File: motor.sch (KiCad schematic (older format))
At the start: 46 parts, among them J16 70543-0003, Q10 PMPB20EN, Q3 PMPB20EN, Q4 PMPB20EN, Q5 PMPB20EN, Q6 PMPB20EN, Q7 PMPB20EN, Q8 PMPB20EN, Q9 PMPB20EN, U6 TMC2160-TA

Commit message: Current snapshot
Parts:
- removed R24: 47k, Resistor_SMD:R_0603_1608Metric, symbol Device:R
- removed R35, R36: 0.15, Resistor_SMD:R_2512_6332Metric, symbol Device:R
- added C41: 100uF, Capacitor_SMD:CP_Elec_6.3x5.7, symbol Device:CP
- C35: renamed from C36; value 220uF -> 100uF; footprint Capacitor_SMD:CP_Elec_8x10 -> Capacitor_SMD:CP_Elec_6.3x5.7
- R32: renamed from R33; value 0.15 -> 0.75; Note (none) -> 0.5 or 1W
- R33: renamed from R34; value 0.15 -> 0.75; Note (none) -> 0.5W or 1W
- renumbered C35 to C34, C37 to C36, C38 to C37, C39 to C38, C40 to C39, C41 to C40, R25 to R24, R26 to R25, R27 to R26, R28 to R27, R29 to R28, R30 to R29, R31 to R30, R32 to R31, R37 to R34, R38 to R35, R39 to R36, R40 to R37
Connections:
- net EN is gone; now on net GND: U6.28 (DRV_ENN)
- net VDD_PWR is gone; now on net VDD24V: D21.1 (K)
- net GND: now also C37.2, C41.2
- net GNDA: no longer C37.2
- net VDD24V: now also C41.1
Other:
- note added: "0.075 Ohm = RMS 3.1A"
- note removed: "0.07 Ohm = RMS 3.4A"

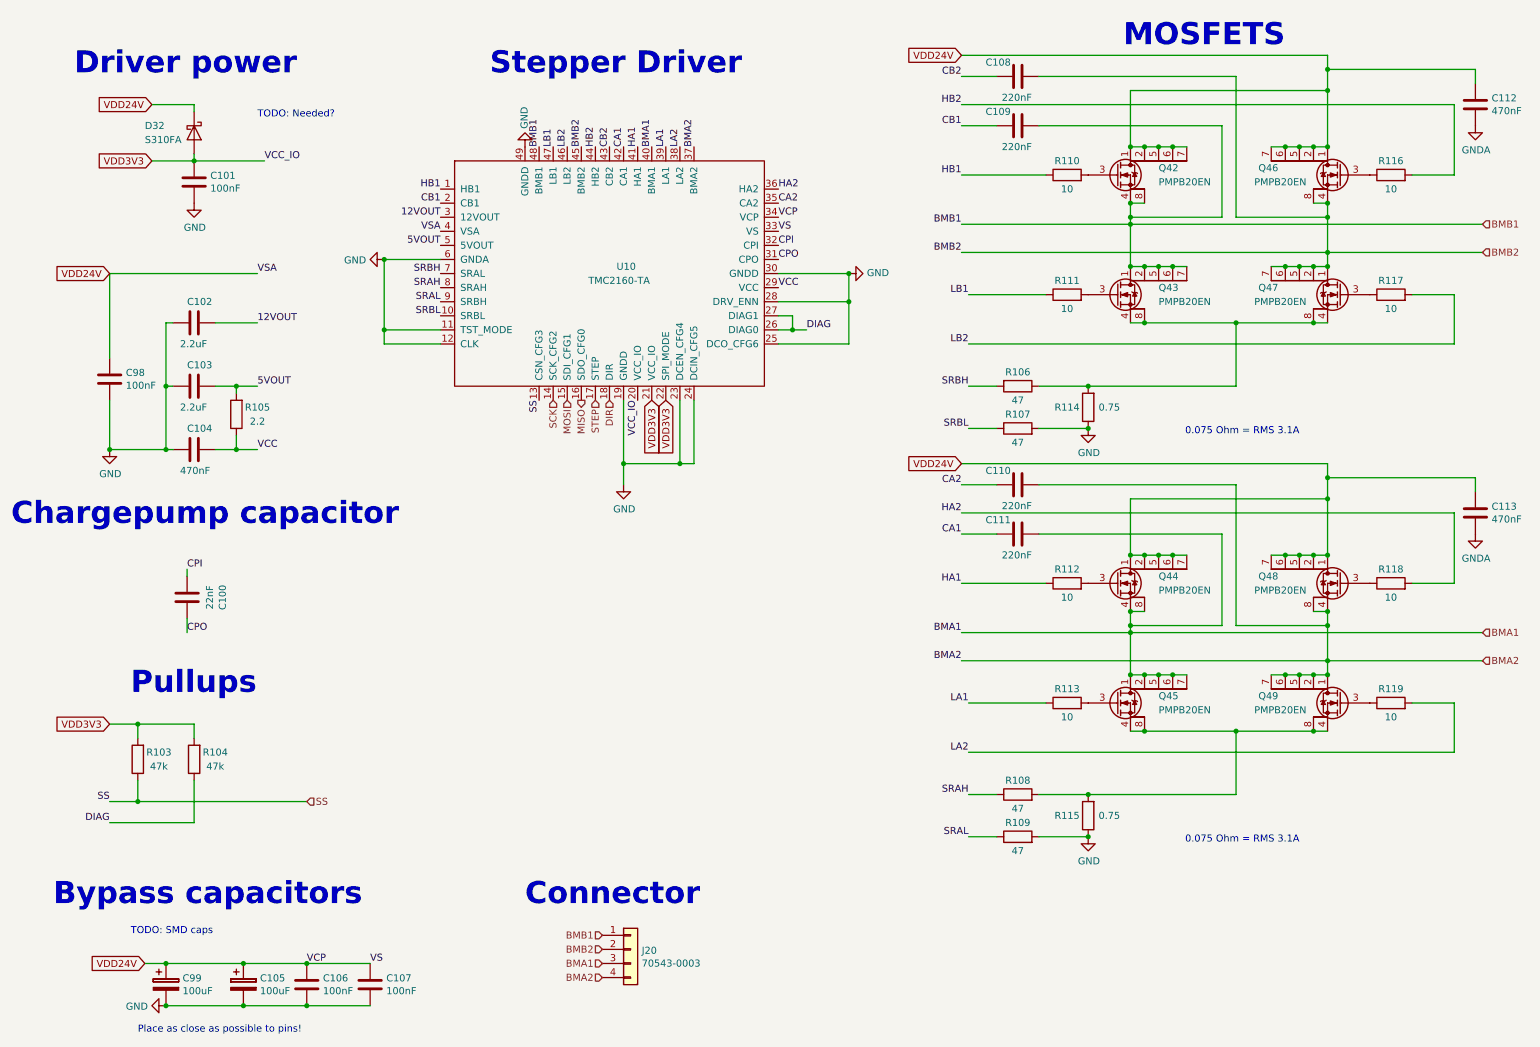
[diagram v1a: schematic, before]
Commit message: Finished general layout and power planes
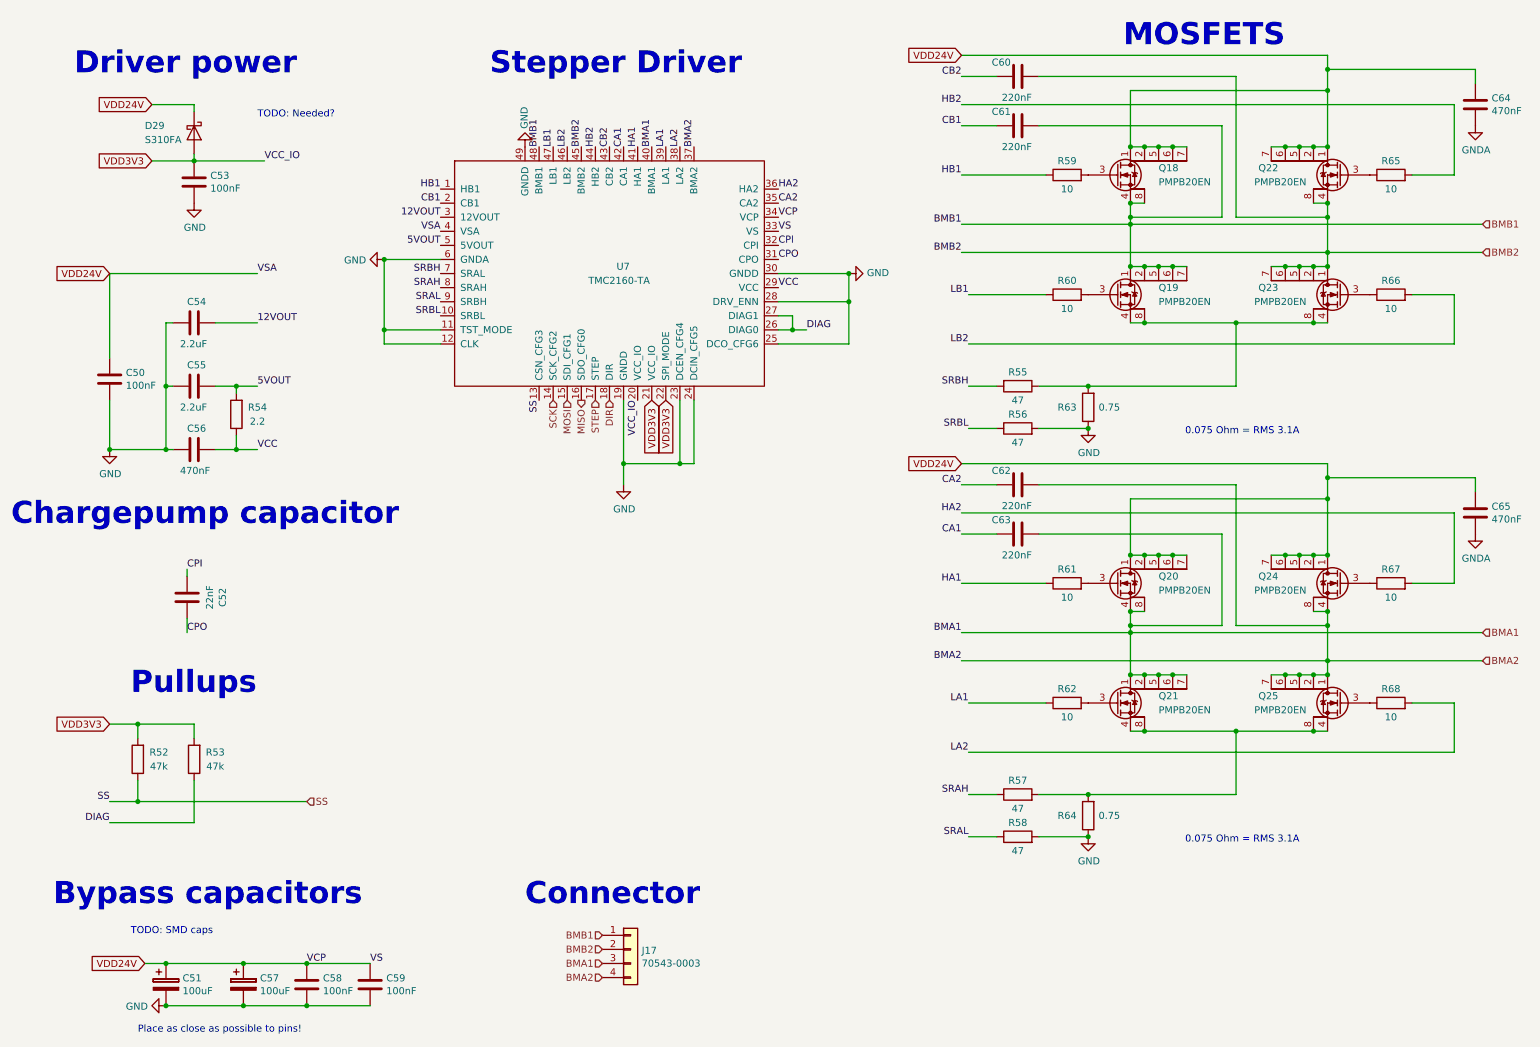
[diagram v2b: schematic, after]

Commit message: Add SD card reader, placed temp connections, fixed stepper placement
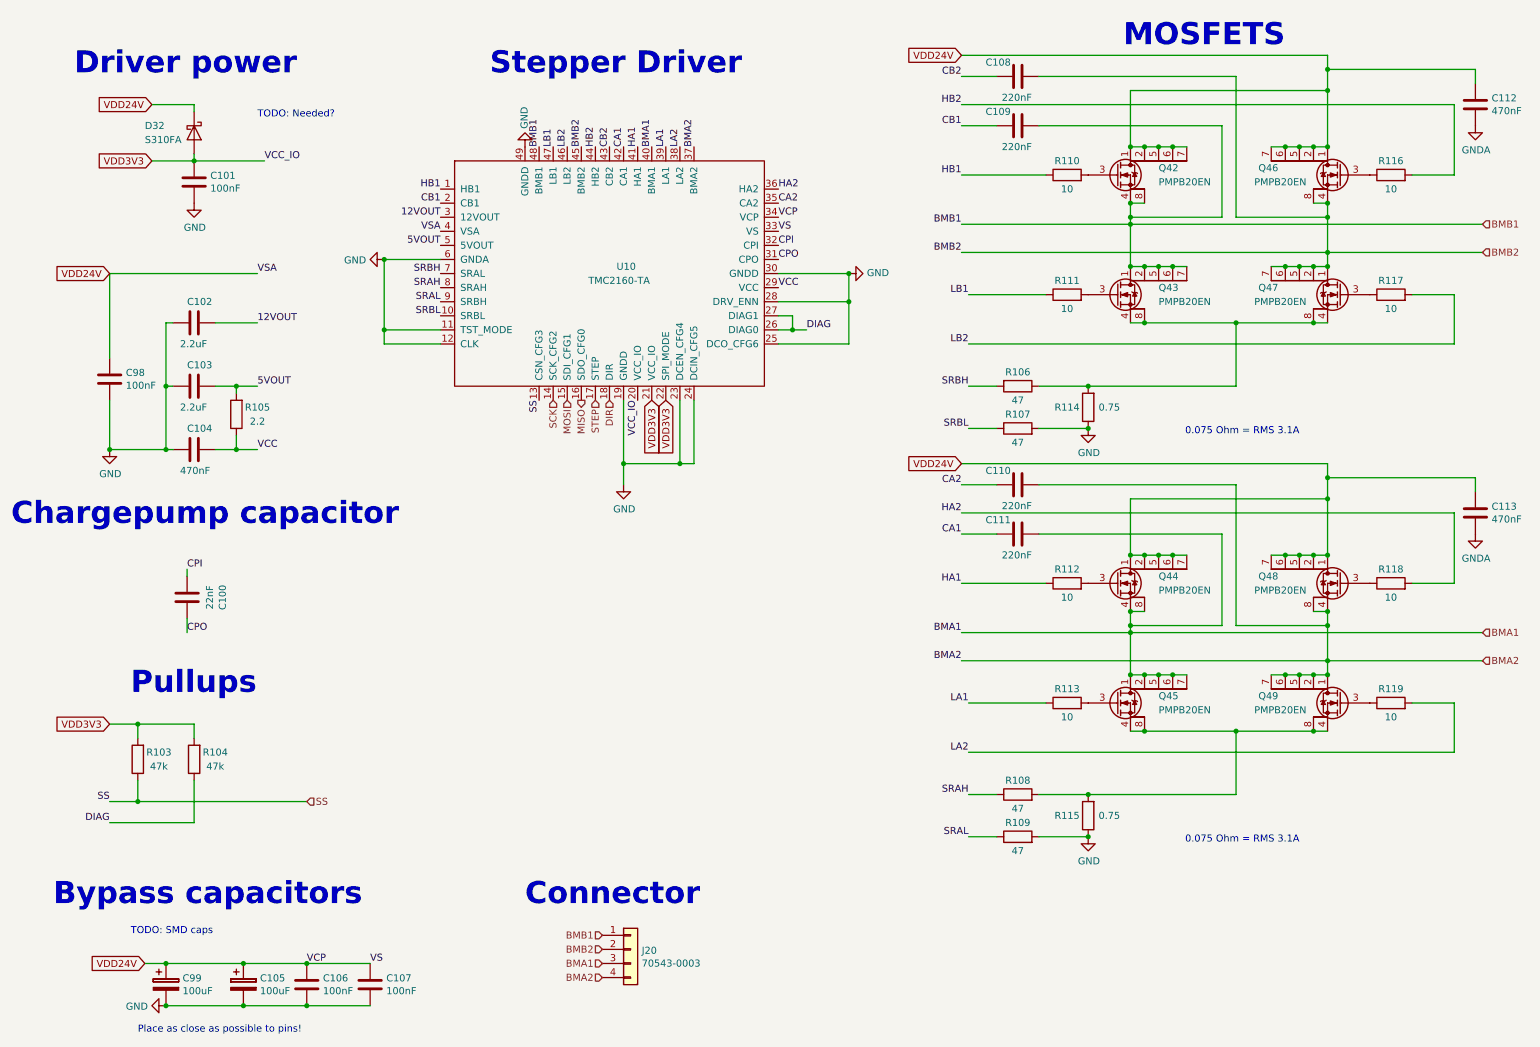
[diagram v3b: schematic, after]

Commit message: Placed some bypass caps
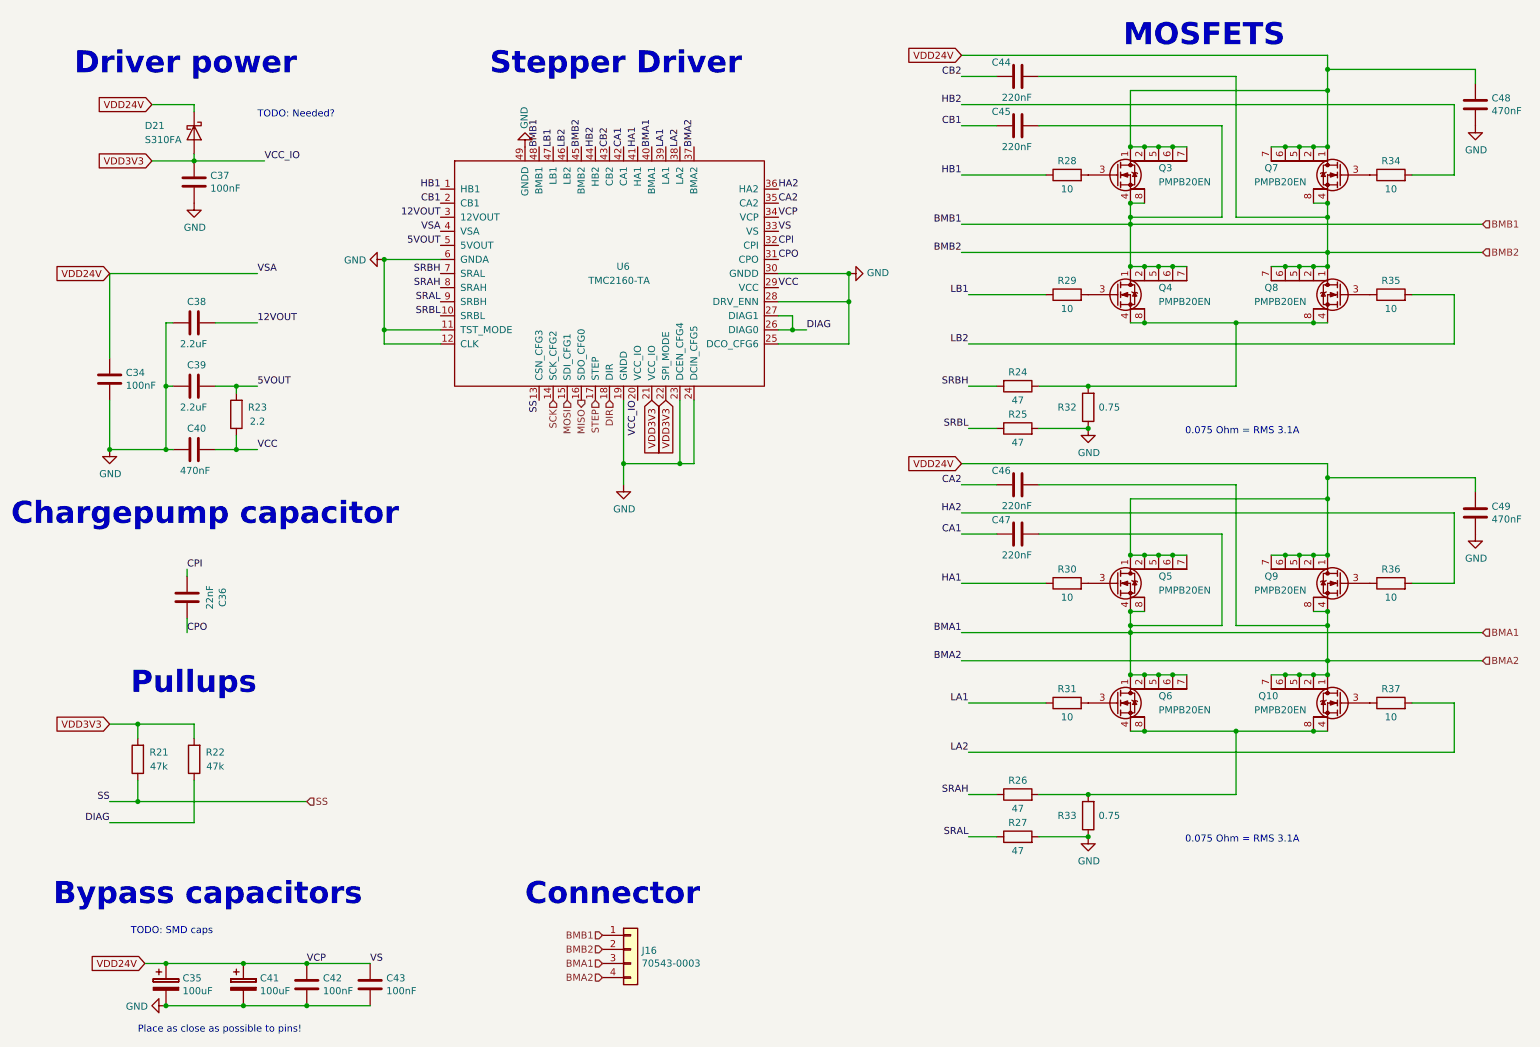
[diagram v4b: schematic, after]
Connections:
- net GNDA is gone; now on net GND: C48.2, C49.2

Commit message: Placed last connectors
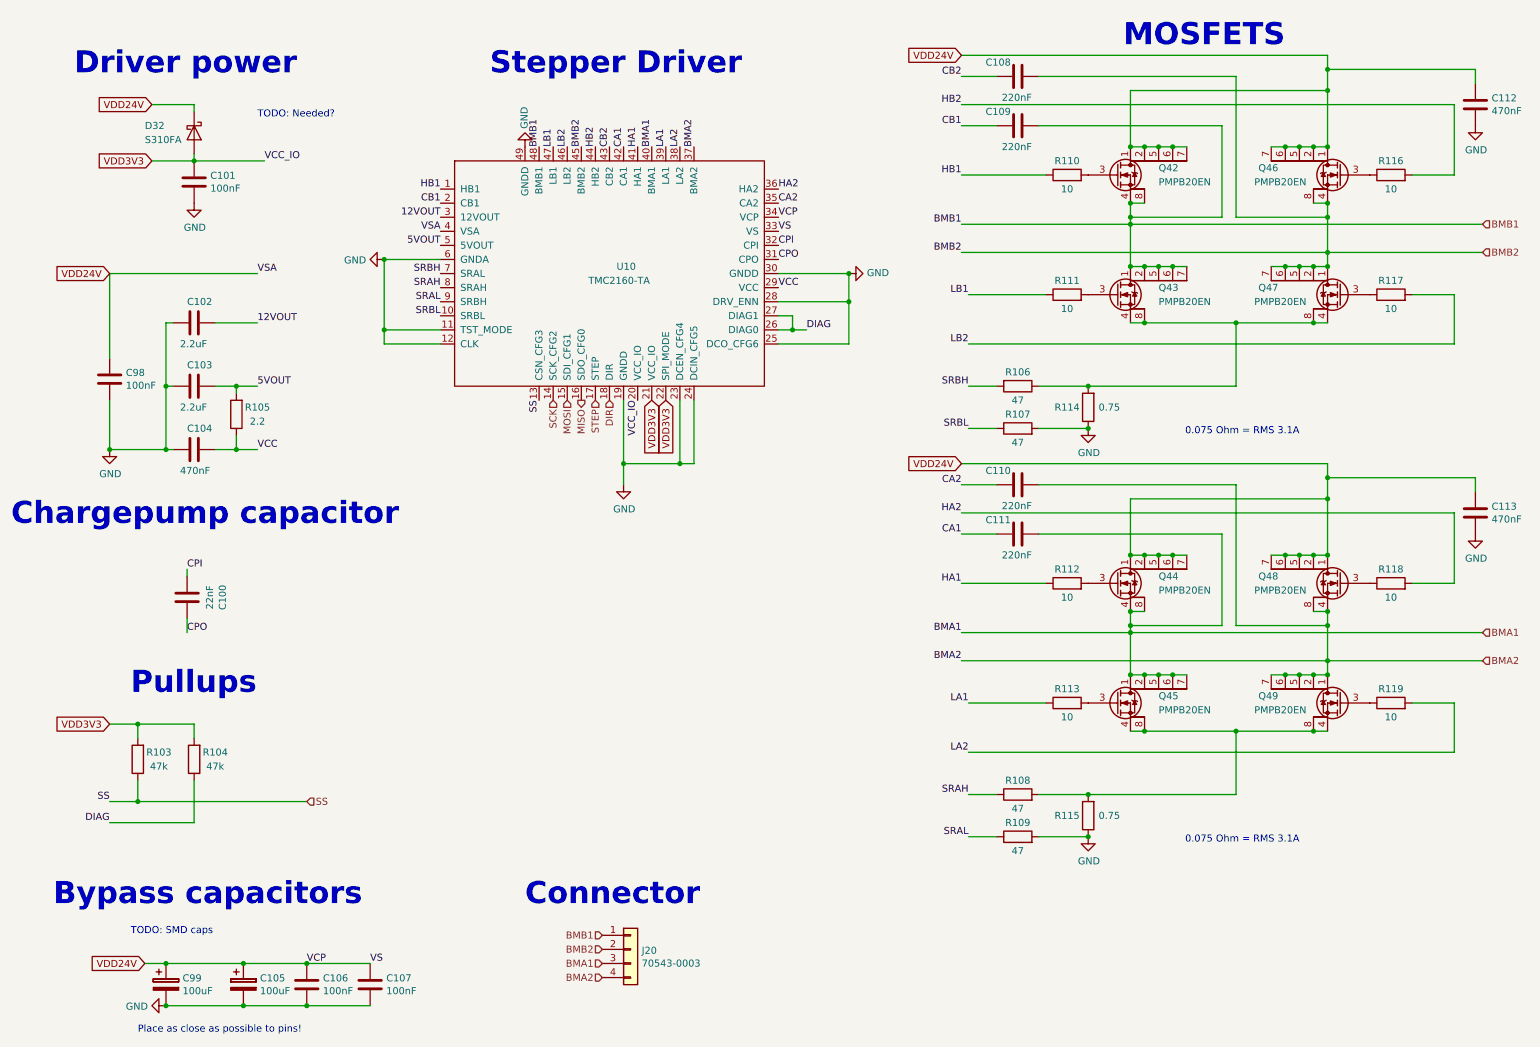
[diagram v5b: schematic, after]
